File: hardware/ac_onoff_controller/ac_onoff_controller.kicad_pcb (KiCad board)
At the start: 4 copper layers, 78.7 x 46.7 mm, 24 parts, among them J1 Conn_02x04_Odd_Even, J2 Conn_01x02, M1 Motor_Servo, Q1 S8050, Q2 S8050, Q3 2SC1815, Q4 S8050, SW1 SW_Push, SW2 SW_Push, SW3 SW_SPST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

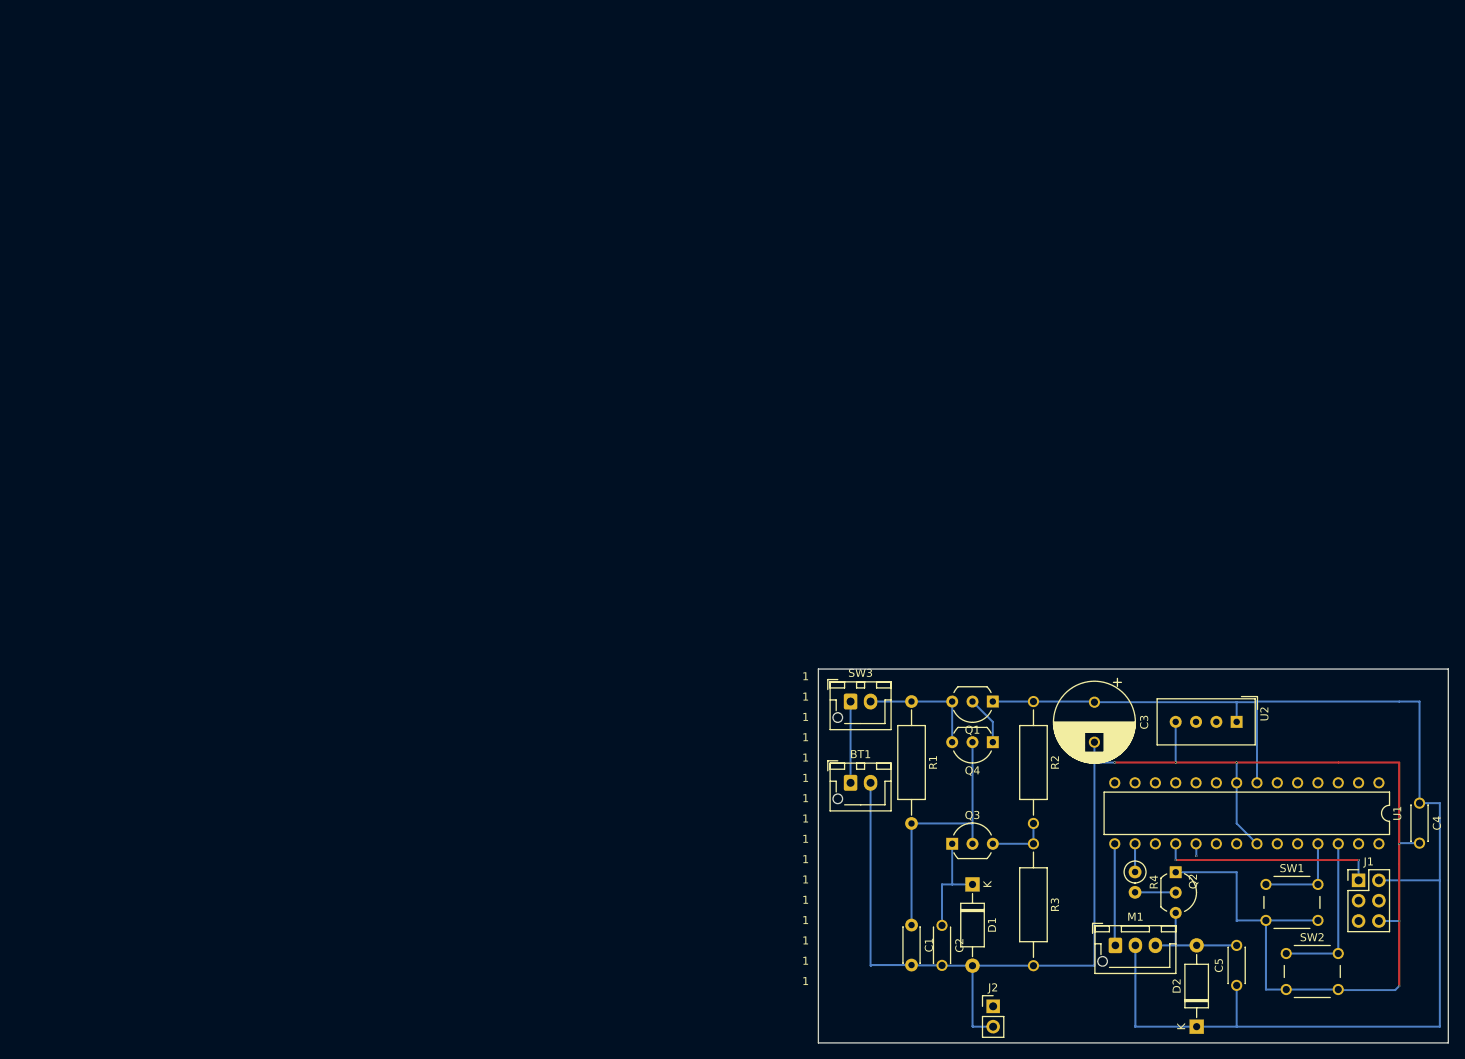
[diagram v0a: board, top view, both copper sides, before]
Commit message: modify footprints etc. for ordering PCBs
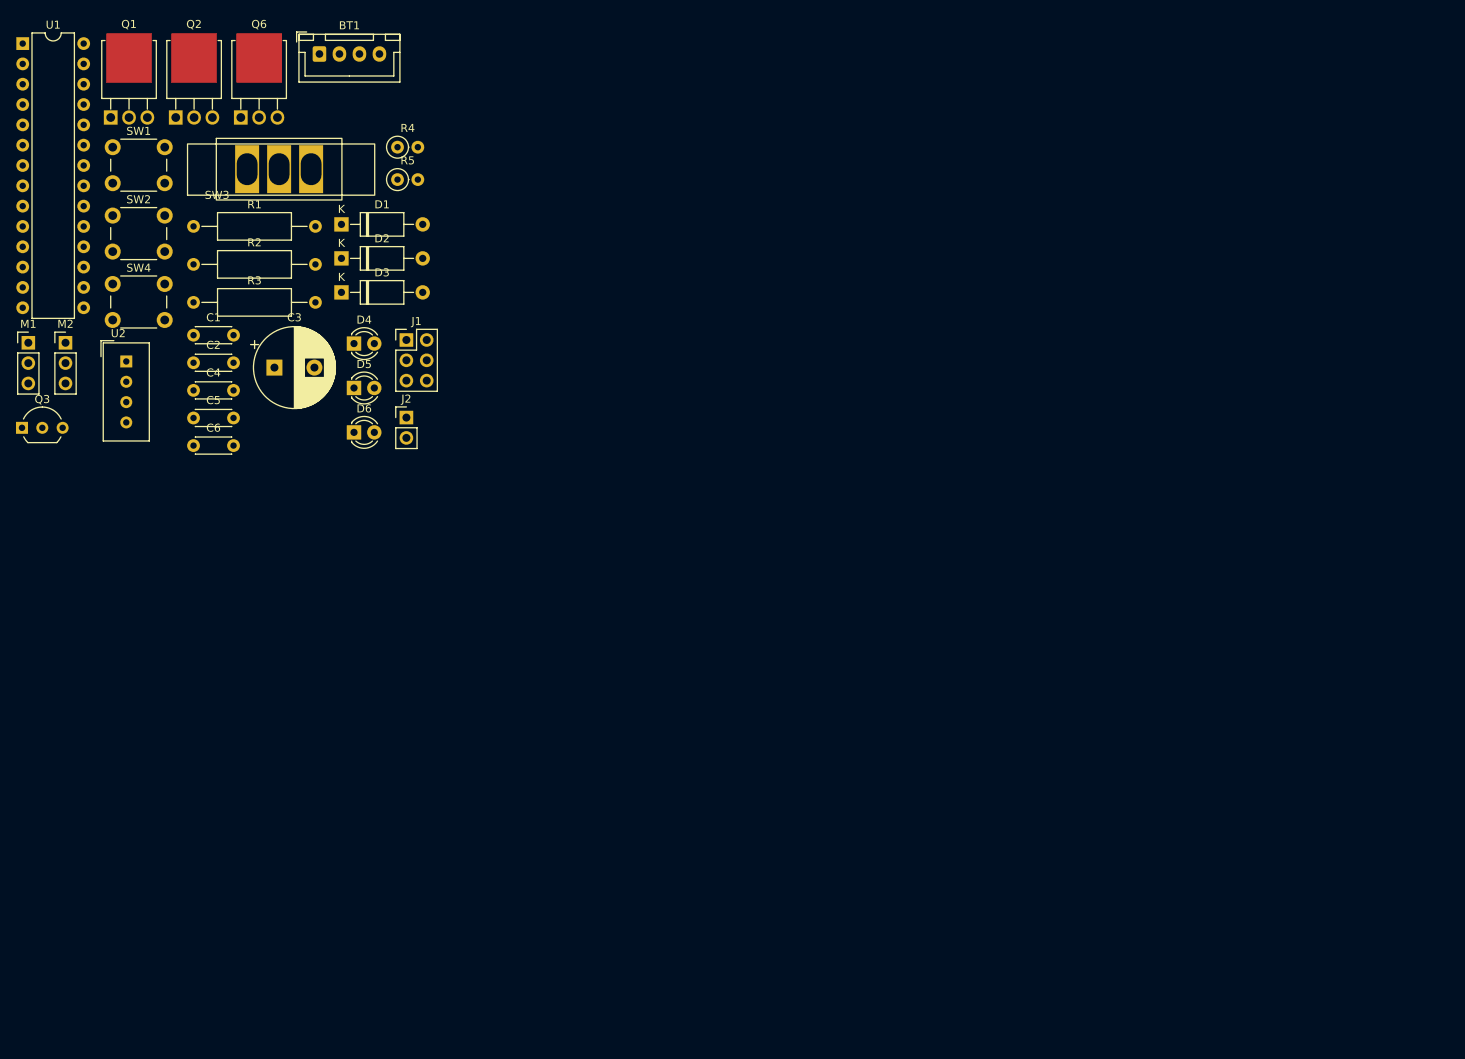
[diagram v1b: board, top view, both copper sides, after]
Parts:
- removed Q4: S8050, Package_TO_SOT_THT:TO-92_Inline_Wide
- added C6: 0.1u, Capacitor_THT:C_Disc_D4.3mm_W1.9mm_P5.00mm, F.Cu at (22.5, 51.8)
- added D3: 1N4148, Diode_THT:D_A-405_P10.16mm_Horizontal, F.Cu at (41.0, 32.7)
- added D4: LED, LED_THT:LED_D3.0mm, F.Cu at (42.5, 39.1)
- added D5: LED, LED_THT:LED_D3.0mm, F.Cu at (42.5, 44.6)
- added D6: LED, LED_THT:LED_D3.0mm, F.Cu at (42.5, 50.2)
- added M2: Motor_Servo, Connector_PinHeader_2.54mm:PinHeader_1x03_P2.54mm_Vertical, F.Cu at (6.47, 39.0)
- added Q6: 2SK4017, ac_onoff_controller:2SK4017, F.Cu at (28.4, 10.8)
- added R5: 500, Resistor_THT:R_Axial_DIN0207_L6.3mm_D2.5mm_P2.54mm_Vertical, F.Cu at (48.0, 18.6)
- added SW4: SW_Push, Button_Switch_THT:SW_PUSH_6mm_H7.3mm, F.Cu at (12.4, 31.6)
- BT1: footprint Connector_JST:JST_XH_B2B-XH-AM_1x02_P2.50mm_Vertical -> Connector_JST:JST_XH_B4B-XH-A_1x04_P2.50mm_Vertical
- M1: footprint Connector_JST:JST_XH_B3B-XH-AM_1x03_P2.50mm_Vertical -> Connector_PinHeader_2.54mm:PinHeader_1x03_P2.54mm_Vertical
- Q1, Q2: value S8050 -> 2SK4017; footprint Package_TO_SOT_THT:TO-92_Inline_Wide -> ac_onoff_controller:2SK4017
- SW3: footprint Connector_JST:JST_XH_B2B-XH-AM_1x02_P2.50mm_Vertical -> ac_onoff_controller:SS-22F25-G4
- U2: value DHT11 -> DHT20; footprint Sensor:Aosong_DHT11_5.5x12.0_P2.54mm -> ac_onoff_controller:Aosong_DHT20
- moved U1 193.1 mm to (1.12, 1.57), turned to 0 degrees
- moved SW2 173.3 mm to (12.4, 23.1)
- moved SW1 171.1 mm to (12.4, 14.5)
- moved C4 161.7 mm to (22.5, 44.9), turned to 0 degrees
- moved Q2 156.6 mm to (20.3, 10.8), turned to 0 degrees
- moved M1 155.4 mm to (1.82, 39.0)
- moved C5 148.4 mm to (22.5, 48.4), turned to 0 degrees
- moved U2 145.9 mm to (14.1, 41.3), turned to 0 degrees
- moved D2 143.7 mm to (41.0, 28.4), turned to 0 degrees
- moved J1 136.9 mm to (49.1, 38.6)
- moved Q1 132.2 mm to (12.1, 10.8), turned to 0 degrees
- moved R4 129.3 mm to (48.0, 14.5), turned to 0 degrees
- moved Q3 127.4 mm to (1.03, 49.6)
- moved R3 124.9 mm to (22.5, 33.9), turned to 0 degrees
- moved R2 118.4 mm to (22.5, 29.2), turned to 0 degrees
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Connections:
- Q1 pad 1: VCC -> Net-(Q1-G)
- Q1 pad 2: Net-(Q1-B) -> Net-(D2-A)
- Q1 pad 3: Net-(Q1-C) -> GND
- Q2 pad 1: GND -> Net-(Q2-G)
- Q2 pad 2: Net-(Q2-B) -> Net-(D3-A)
- Q2 pad 3: Net-(D2-A) -> GND
- R1 pad 1: Net-(Q1-C) -> Net-(Q6-D)
- R4 pad 2: Net-(Q2-B) -> Net-(Q1-G)
- SW3 pad 1: Net-(BT1-+) -> Net-(Q6-D)
- SW3 pad 2: Net-(Q1-C) -> Net-(BT1-+)
- U1 pad 14: DHT11_DATA -> unconnected-(U1-PB0-Pad14)
- U1 pad 23: unconnected-(U1-PC0-Pad23) -> PC0
- U1 pad 27: unconnected-(U1-PC4-Pad27) -> SDA
- U1 pad 28: unconnected-(U1-PC5-Pad28) -> SCL
- U1 pad 4: unconnected-(U1-PD2-Pad4) -> STON
- U1 pad 5: unconnected-(U1-PD3-Pad5) -> STOFF
- U1 pad 6: unconnected-(U1-PD4-Pad6) -> TGL
- U2 pad 2: DHT11_DATA -> SDA
- U2 pad 3: unconnected-(U2-NC-Pad3) -> GND
- U2 pad 4: GND -> SCL
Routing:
- net GND: track 225.9 -> 0.00 mm, vias 6 -> 0
- net VCC: track 170.3 -> 0.00 mm
- net Net-(J2-Pin_1): track 91.5 -> 0.00 mm
- net /MOSI: track 38.2 -> 0.00 mm
- net Net-(Q3-C): track 33.0 -> 0.00 mm
- net /RST: track 30.0 -> 0.00 mm
- net /MISO: track 27.4 -> 0.00 mm, vias 2 -> 0
- net /SCK: track 27.4 -> 0.00 mm, vias 1 -> 0
- net DHT11_DATA: track 20.3 -> 0.00 mm
- net Net-(U1-PC3): track 20.2 -> 0.00 mm
- net Net-(Q1-C): track 15.3 -> 0.00 mm
- net Net-(D2-A): track 14.2 -> 0.00 mm
- net Net-(D1-K): track 14.0 -> 0.00 mm
- net Net-(M1-PWM): track 12.7 -> 0.00 mm
- net Net-(U1-PC2): track 11.6 -> 0.00 mm
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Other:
- board outline removed
- board text removed: "1"

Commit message: wip: add a new pcb design for ordering to vendors
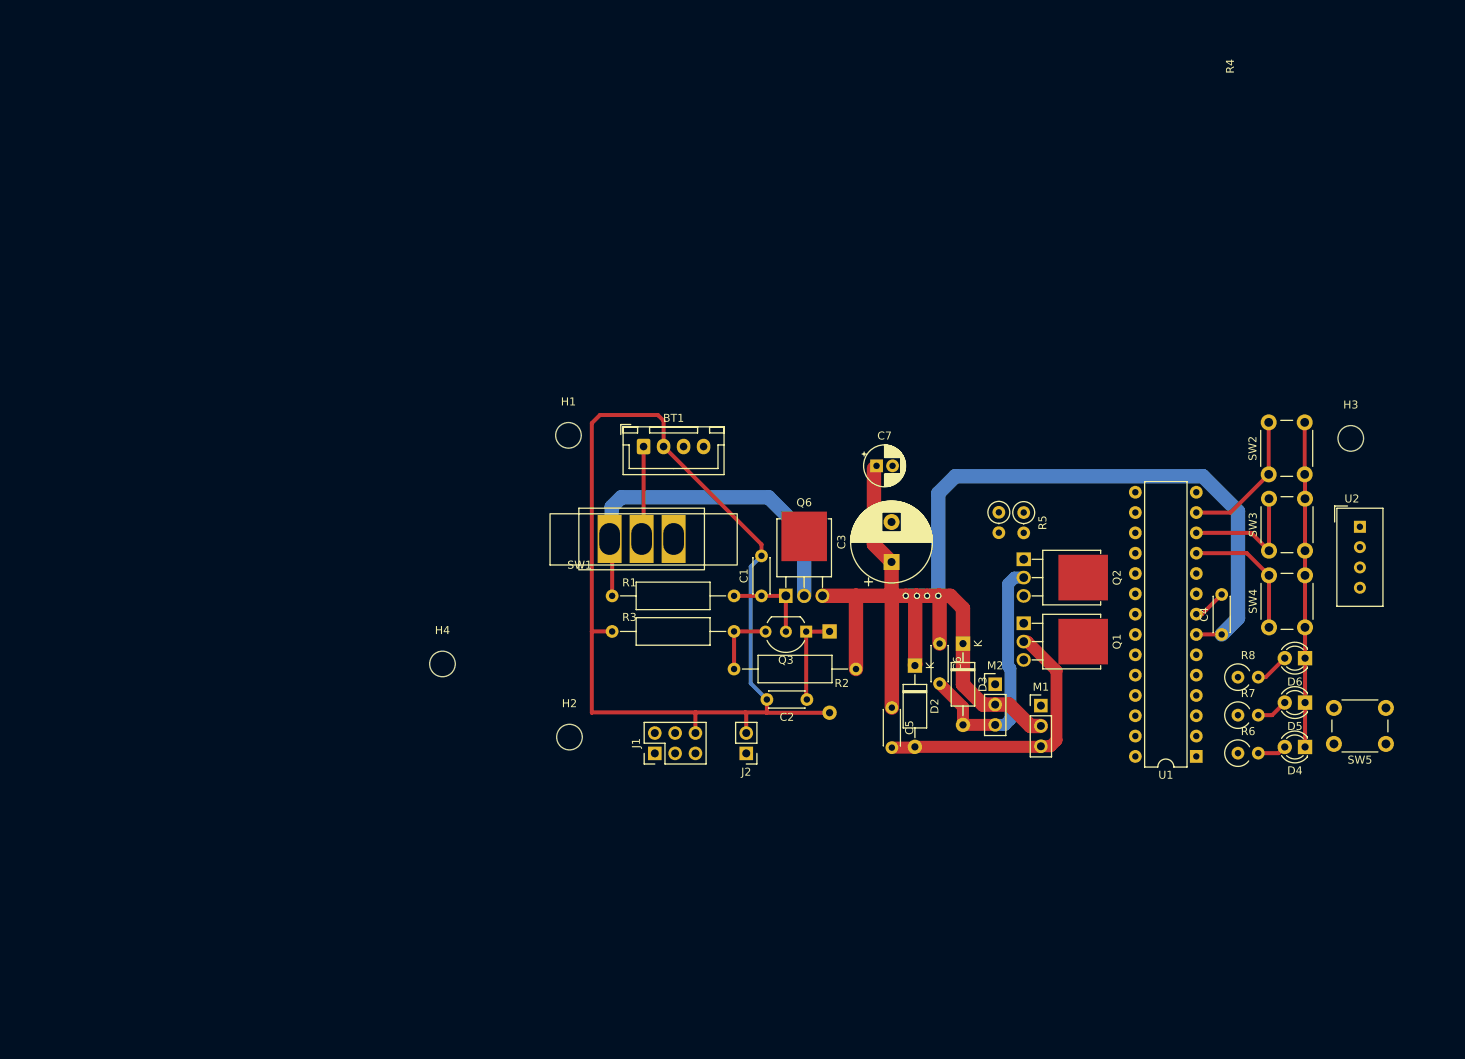
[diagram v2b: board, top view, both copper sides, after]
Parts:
- added C7: 10u, Capacitor_THT:CP_Radial_D5.0mm_P2.00mm, F.Cu at (107.9, 54.4)
- added H1: MountingHole, MountingHole:MountingHole_3.2mm_M3, F.Cu at (69.3, 50.5)
- added H2: MountingHole, MountingHole:MountingHole_3.2mm_M3, F.Cu at (69.5, 88.3)
- added H3: MountingHole, MountingHole:MountingHole_3.2mm_M3, F.Cu at (167.1, 50.9)
- added H4: MountingHole, MountingHole:MountingHole_3.2mm_M3, F.Cu at (53.6, 79.1)
- added R6: 22k, Resistor_THT:R_Axial_DIN0309_L9.0mm_D3.2mm_P2.54mm_Vertical, F.Cu at (153.0, 90.3)
- added R7: 22k, Resistor_THT:R_Axial_DIN0309_L9.0mm_D3.2mm_P2.54mm_Vertical, F.Cu at (153.0, 85.5)
- added R8: 22k, Resistor_THT:R_Axial_DIN0309_L9.0mm_D3.2mm_P2.54mm_Vertical, F.Cu at (153.0, 80.8)
- added SW5: SW_Push, Button_Switch_THT:SW_PUSH_6mm_H7.3mm, F.Cu at (171.5, 89.1)
- D1: moved to B.Cu
- SW1: value SW_Push -> SW_SPST; footprint Button_Switch_THT:SW_PUSH_6mm_H7.3mm -> ac_onoff_controller:SS-22F25-G4
- SW3: value SW_SPST -> SW_Push; footprint ac_onoff_controller:SS-22F25-G4 -> Button_Switch_THT:SW_PUSH_6mm_H7.3mm
- moved U1 171.6 mm to (147.8, 90.7), turned to 180 degrees
- moved U2 155.6 mm to (168.3, 62.0)
- moved SW4 150.8 mm to (156.9, 74.5), turned to 90 degrees
- moved SW2 148.1 mm to (156.9, 55.4), turned to 90 degrees
- moved SW3 138.6 mm to (156.9, 65.0), turned to 90 degrees
- moved M1 134.5 mm to (128.4, 84.3)
- moved C4 132.1 mm to (151.0, 75.4), turned to 90 degrees
- moved Q1 130.5 mm to (126.2, 74.0), turned to -90 degrees
- moved D4 129.1 mm to (161.4, 89.5), turned to 180 degrees
- moved D5 125.2 mm to (161.4, 83.9), turned to 180 degrees
- moved M2 123.8 mm to (122.7, 81.7)
- moved D6 122.2 mm to (161.4, 78.4), turned to 180 degrees
- moved Q2 119.5 mm to (126.2, 66.0), turned to -90 degrees
- moved Q3 101.3 mm to (99.1, 75.1), turned to 180 degrees
- moved R2 97.0 mm to (105.3, 79.8), turned to 180 degrees
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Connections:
- D4 pad 2: STON -> Net-(D4-A)
- D5 pad 2: STOFF -> Net-(D5-A)
- D6 pad 2: TGL -> Net-(D6-A)
- SW1 pad 1: Net-(U1-PC2) -> Net-(Q6-D)
- SW1 pad 2: GND -> Net-(BT1-+)
- SW2 pad 1: Net-(U1-PC3) -> Net-(U1-PD7)
- SW3 pad 1: Net-(Q6-D) -> Net-(U1-PD6)
- SW3 pad 2: Net-(BT1-+) -> GND
- SW4 pad 1: /RST -> Net-(U1-PD5)
- U1 pad 11: unconnected-(U1-PD5-Pad11) -> Net-(U1-PD5)
- U1 pad 12: unconnected-(U1-PD6-Pad12) -> Net-(U1-PD6)
- U1 pad 13: unconnected-(U1-PD7-Pad13) -> Net-(U1-PD7)
- U1 pad 25: Net-(U1-PC2) -> unconnected-(U1-PC2-Pad25)
- U1 pad 26: Net-(U1-PC3) -> unconnected-(U1-PC3-Pad26)
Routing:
- net VCC: track 0.00 -> 171.6 mm, vias 0 -> 4
- net GND: track 0.00 -> 171.2 mm
- net Net-(Q6-D): track 0.00 -> 45.4 mm
- net Net-(D2-A): track 0.00 -> 35.3 mm
- net Net-(D3-A): track 0.00 -> 31.9 mm
- net Net-(U1-PD7): track 0.00 -> 17.5 mm
- net Net-(U1-PD5): track 0.00 -> 16.7 mm
- net Net-(U1-PD6): track 0.00 -> 16.5 mm
- net Net-(BT1-+): track 0.00 -> 11.6 mm
- net Net-(D1-K): track 0.00 -> 11.5 mm
- net Net-(Q3-C): track 0.00 -> 11.0 mm
- net Net-(Q3-B): track 0.00 -> 8.64 mm
- net Net-(D6-A): track 0.00 -> 4.29 mm
- net Net-(D5-A): track 0.00 -> 3.96 mm
- net Net-(D4-A): track 0.00 -> 3.63 mm
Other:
- copper layers 4 -> 2

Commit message: add a new pcb design for ordering to vendors
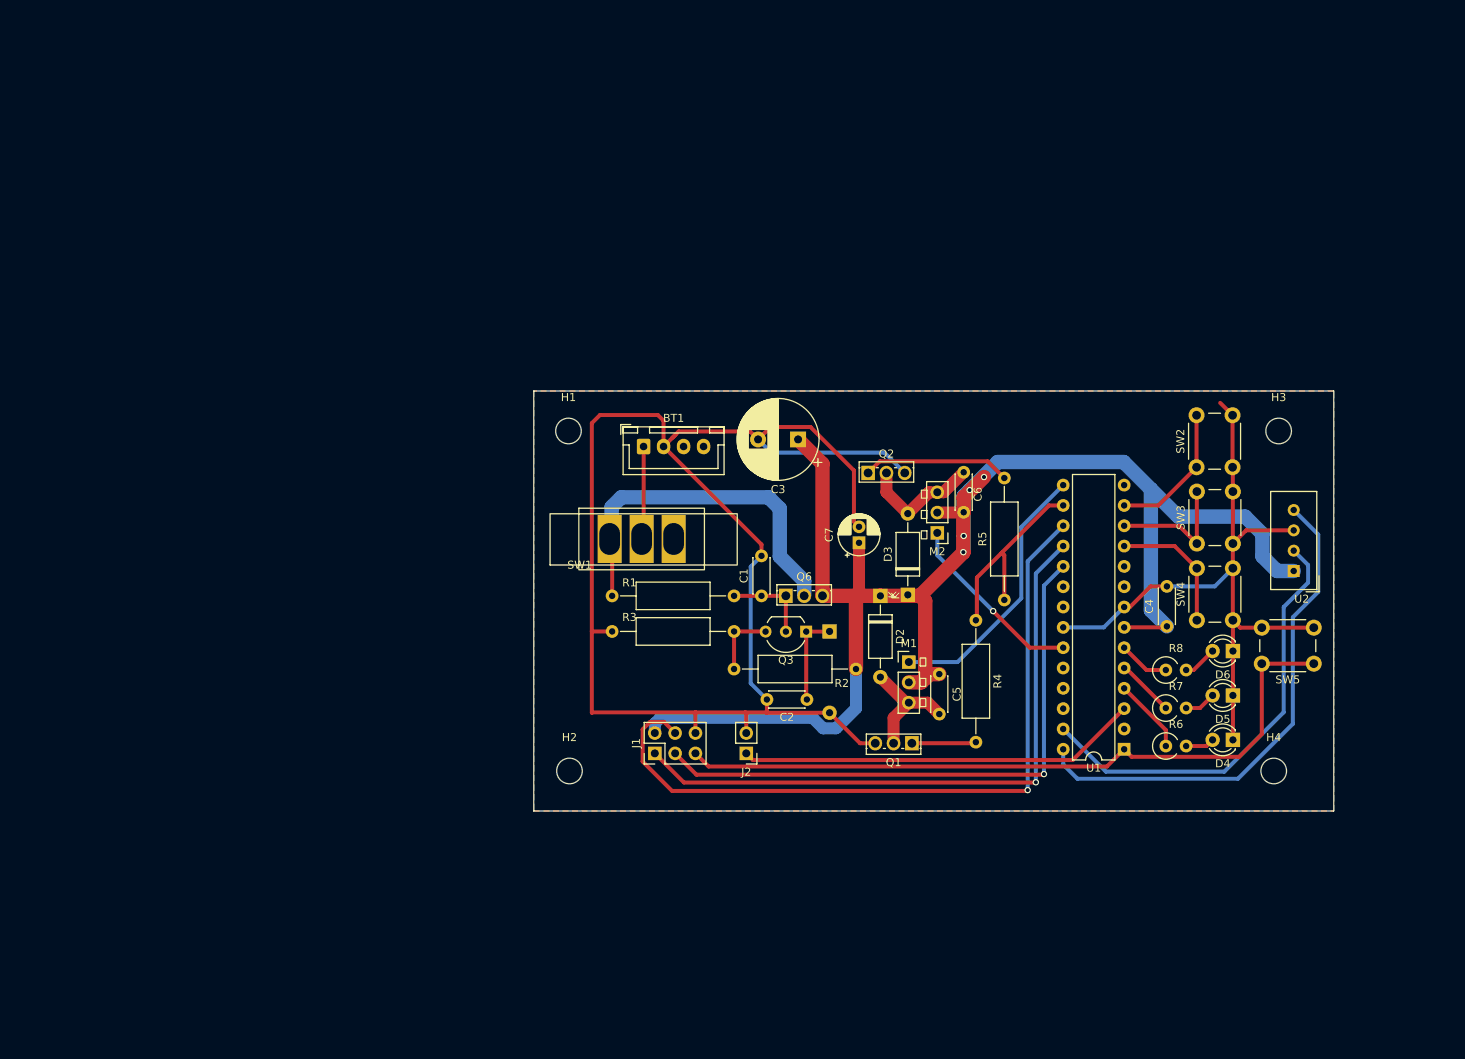
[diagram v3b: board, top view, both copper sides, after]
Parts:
- Q1, Q2, Q6: footprint ac_onoff_controller:2SK4017 -> Package_TO_SOT_THT:TO-251-3_Vertical
- R4, R5: footprint Resistor_THT:R_Axial_DIN0207_L6.3mm_D2.5mm_P2.54mm_Vertical -> Resistor_THT:R_Axial_DIN0309_L9.0mm_D3.2mm_P15.24mm_Horizontal
- moved H4 104.8 mm to (157.5, 92.5)
- moved Q2 22.2 mm to (106.8, 55.2), turned to 0 degrees
- moved Q1 20.5 mm to (112.3, 89.0), turned to 180 degrees
- moved M2 20.3 mm to (115.4, 62.7), turned to 180 degrees
- moved C3 19.3 mm to (98.0, 51.1), turned to 180 degrees
- moved M1 17.4 mm to (111.9, 78.9)
- moved C6 16.7 mm to (118.7, 60.2), turned to 90 degrees
- moved R4 13.8 mm to (120.3, 73.7)
- moved SW5 13.5 mm to (162.5, 79.1)
- moved R5 11.2 mm to (123.8, 71.1), turned to 90 degrees
- moved U2 9.95 mm to (160.0, 67.5), turned to 180 degrees
- moved C7 9.87 mm to (105.7, 64.0), turned to 90 degrees
- moved D2 9.72 mm to (108.3, 70.6)
- moved D3 9.21 mm to (111.8, 70.5), turned to 90 degrees
- moved H3 9.06 mm to (158.1, 50.0)
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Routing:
- net GND: track 171.2 -> 275.5 mm
- net /MOSI: track 0.00 -> 93.6 mm, vias 0 -> 1
- net /RST: track 0.00 -> 89.2 mm
- net /MISO: track 0.00 -> 80.1 mm, vias 0 -> 1
- net /SCK: track 0.00 -> 74.2 mm, vias 0 -> 1
- net SCL: track 0.00 -> 63.5 mm
- net SDA: track 0.00 -> 55.1 mm
- net Net-(J2-Pin_1): track 0.00 -> 50.3 mm
- net Net-(M1-PWM): track 0.00 -> 33.7 mm
- net VCC: track 171.6 -> 199.1 mm
- net Net-(U1-PB2): track 0.00 -> 25.9 mm
- net PC0: track 0.00 -> 23.3 mm, vias 0 -> 1
- net Net-(D2-A): track 35.3 -> 15.1 mm
- net Net-(Q2-G): track 0.00 -> 18.5 mm
- net Net-(D3-A): track 31.9 -> 15.3 mm
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- added copper zone on B.Cu, net GND
- added copper zone on F.Cu, net GND
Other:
- board outline added: 100 x 52.5 mm
- board text added: "橙"
- board text added: "茶"
- board text added: "赤"

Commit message: use trim register for voltage regulator feedback
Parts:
- removed R2: 5.2k, Resistor_THT:R_Axial_DIN0309_L9.0mm_D3.2mm_P15.24mm_Horizontal
- removed R3: 10k, Resistor_THT:R_Axial_DIN0309_L9.0mm_D3.2mm_P15.24mm_Horizontal
- added RV1: R_Potentiometer_Trim, ac_onoff_controller:GF063P, F.Cu at (85.8, 76.4)
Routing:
- net GND: track 275.5 -> 283.4 mm
- net Net-(Q3-B): track 8.64 -> 14.4 mm
- net VCC: track 199.1 -> 203.1 mm, vias 4 -> 5
